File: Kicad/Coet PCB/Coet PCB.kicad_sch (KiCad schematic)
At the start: 2 parts, among them U1 BNO055 Stemma, U2 Teensy4.1

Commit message: kicad components
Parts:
- added U3: BMP280 Stemma, BMP280:BMP280, symbol BMP280:BMP280
- added U4: MP1584EN, MP1584EN:MP1584EN, symbol MP1584EN:MP1584EN
- added U5: XL4015_DC, XL4015_DC:XL4015, symbol XL4015 DC-DC:XL4015_DC
- U1: footprint Bno055:BNO055 -> BNO055:BNO055
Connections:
- net at U1.7 (INT): no longer U2.1 (GND)
- net at U1.8 (ADR): no longer U2.4 (2_OUT2)

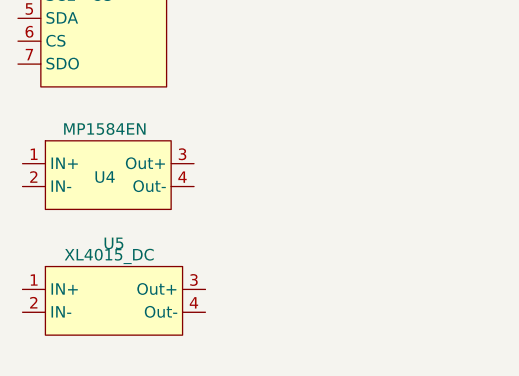
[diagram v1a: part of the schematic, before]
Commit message: Added the next libraries to Kicad: Teensy4.1, Bno055, Bmp280, MP1584EN, XL4015DC
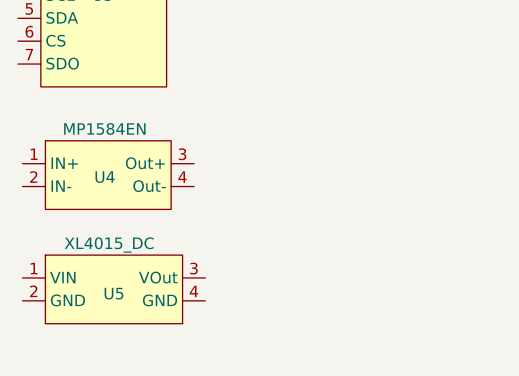
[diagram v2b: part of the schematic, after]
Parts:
- U5: footprint XL4015_DC:XL4015 -> XL4015DC:XL4015 DC-DC
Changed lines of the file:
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@@
 	(symbol
 		(lib_id "XL4015 DC-DC:XL4015_DC")
-		(at 72.39 121.92 0)
+		(at 72.39 120.65 0)
 		(unit 1)
 		(body_style 1)
@@
 		(fields_autoplaced yes)
 		(property "Reference" "U5"
-			(at 72.39 115.57 0)
-			(show_name no)
-			(do_not_autoplace no)
-			(effects
-				(font
-					(size 1.27 1.27)
-				)
-			)
-		)
-		(property "Value" "XL4015_DC"
-			(at 71.882 116.84 0)
+			(at 72.39 121.158 0)
 			(show_name no)
 			(do_not_autoplace yes)
@@
 			)
 		)
-		(property "Footprint" "XL4015_DC:XL4015"
-			(at 72.39 121.92 0)
+		(property "Value" "XL4015_DC"
+			(at 71.882 115.57 0)
+			(show_name no)
+			(do_not_autoplace yes)
+			(effects
+				(font
+					(size 1.27 1.27)
+				)
+			)
+		)
+		(property "Footprint" "XL4015DC:XL4015 DC-DC"
+			(at 72.39 120.65 0)
 			(hide yes)
 			(show_name no)
@@
 		)
 		(property "Datasheet" "https://components101.com/modules/xl4015-dc-dc-converter-module"
-			(at 72.39 121.92 0)
+			(at 72.39 120.65 0)
 			(hide yes)
 			(show_name no)
@@
 		)
 		(property "Description" ""
-			(at 72.39 121.92 0)
+			(at 72.39 120.65 0)
 			(hide yes)
 			(show_name no)
@@
 		(pin "1"
 		)
+		(pin "2"
+		)
 		(pin "3"
 		)
-		(pin "2"
-		)
 		(pin "4"

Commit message: He acabat les conecions del esquema!
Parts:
- added BZ1: Buzzer, Buzzer_Beeper:Buzzer_TDK_PS1240P02BT_D12.2mm_H6.5mm, symbol Device:Buzzer
- added C1_100uf1, C1_470uf1: C_US, Capacitor_SMD:CP_Elec_8x5.4, symbol Device:C_US
- added D1: LED_ABGR, LED_THT:LED_D5.0mm-4_RGB_Wide_Pins, symbol Device:LED_ABGR
- added M1: TVC1, Connector_PinHeader_1.00mm:PinHeader_1x03_P1.00mm_Vertical, symbol Motor:Motor_Servo
- added M2: TVC2, Connector_PinHeader_1.00mm:PinHeader_1x03_P1.00mm_Vertical, symbol Motor:Motor_Servo
- added M3: Parachute, Connector_PinHeader_1.00mm:PinHeader_1x03_P1.00mm_Vertical, symbol Motor:Motor_Servo
- added R1: R1, Resistor_THT:R_Axial_DIN0207_L6.3mm_D2.5mm_P10.16mm_Horizontal, symbol Device:R
- added R2: R20, Resistor_THT:R_Axial_DIN0207_L6.3mm_D2.5mm_P10.16mm_Horizontal, symbol Device:R
- added R3: R67, Resistor_THT:R_Axial_DIN0207_L6.3mm_D2.5mm_P10.16mm_Horizontal, symbol Device:R
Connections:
- net +BATT: now reaches U5.1 (VIN)
- net +BATT: now also U4.1 (VIN)
- net GND: now reaches U5.2 (GND)
- net GND: now also U4.2 (GND)
- net at U5.3 (VOut): now also C1_470uf1.1
- net at U5.4 (GND): now also U2.1 (GND), U4.4 (GND), BZ1.2 (-), D1.1 (A), M1.3 (-), M2.3 (-), M3.3 (-)
- net at U4.3 (VOut): now also C1_100uf1.1
- net at U1.1 (Vin): now also U2.48 (VIN), C1_100uf1.2
- net at U1.3 (GND): now also U2.47 (GND)
- net at U1.4 (SCL): now also U2.41 (19_A5_SCL)
- net at U1.5 (SDA): now also U2.40 (18_A4_SDA)
- net at U2.10 (8_TX2_IN1): now also R1.1
- net at U2.11 (9_OUT1C): now also R2.1
- net at U2.12 (10_CS_MQSR): now also R3.1
- net at U2.4 (2_OUT2): now also BZ1.1 (+)
- new net: C1_470uf1.2, M1.2 (+), M2.2 (+), M3.2 (+)
- new net: D1.3 (GK), R2.2
- new net: D1.2 (BK), R1.2
- new net: D1.4 (RK), R3.2
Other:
- moved on the sheet: U1, U2, U5
